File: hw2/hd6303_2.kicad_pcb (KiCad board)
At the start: 2 copper layers, 90.2 x 70.1 mm, 29 parts, among them J1 Conn_02x20_Odd_Even, J2 Conn_02x06_Odd_Even, J3 Screw_Terminal_01x02, SW1 SW_Push, U2 MAX708, U3 27C512, U4 HD6303RP, U5 HM62256BLP-7, U6 GAL16V8, Y1 4.9152M

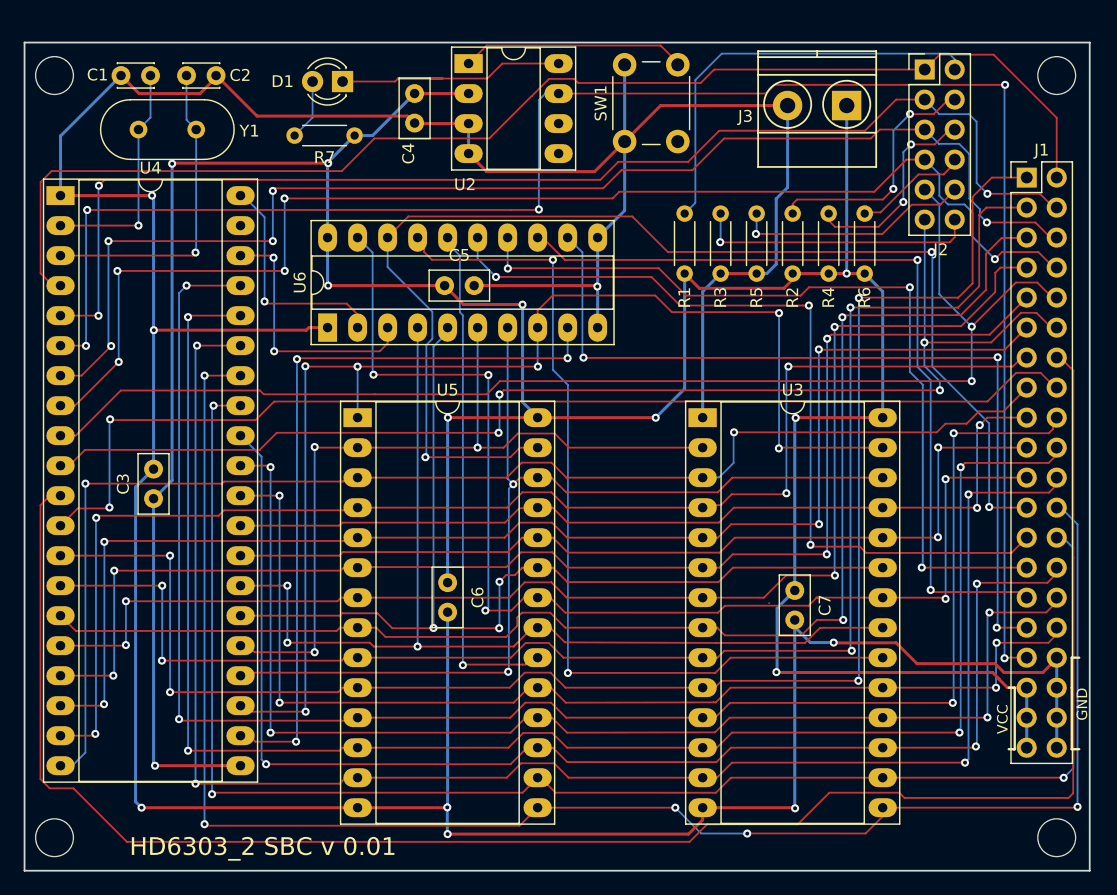
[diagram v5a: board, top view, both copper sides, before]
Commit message: reroute a couple of traces, silkscreen additions
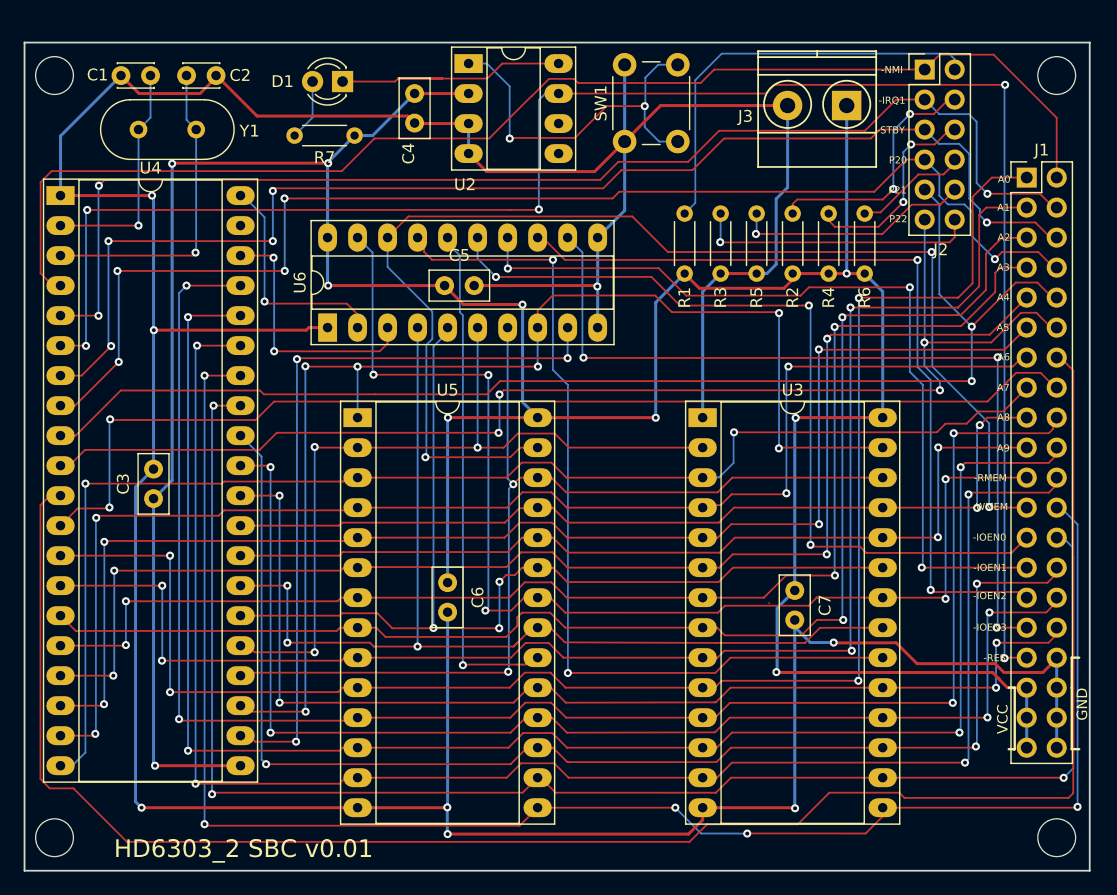
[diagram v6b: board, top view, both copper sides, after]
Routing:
- net Net-(SW1-Pad2): track 19.1 -> 32.3 mm, vias 0 -> 2
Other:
- board text added: "-IOEN0"
- board text added: "-IOEN1"
- board text added: "-IOEN2"
- board text added: "-IOEN3"
- board text added: "-IRQ1"
- board text added: "-NMI"
- board text added: "-RES"
- board text added: "-RMEM"
- board text added: "-STBY"
- board text added: "-WMEM"
- board text added: "A0"
- board text added: "A1"
- board text added: "A2"
- board text added: "A3"
- board text added: "A4"
- board text added: "A5"
- board text added: "A6"
- board text added: "A7"
- board text added: "A8"
- board text added: "A9"
- board text added: "HD6303_2 SBC v0.01"
- board text added: "P20"
- board text added: "P21"
- board text added: "P22"
- board text removed: "HD6303_2 SBC v 0.01"
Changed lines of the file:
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@@
-(kicad_pcb (version 4) (host pcbnew 4.0.7-e2-6376~58~ubuntu16.04.1)
+(kicad_pcb (version 4) (host pcbnew 4.0.2+dfsg1-stable)
   (general
     (links 155)
-    (no_connects 1)
-    (area 66.144857 85.645 178.203143 159.819)
+    (no_connects 0)
+    (area 66.069857 85.495 178.278143 159.719)
     (thickness 1.6)
-    (drawings 15)
-    (tracks 1157)
+    (drawings 38)
+    (tracks 1171)
     (zones 0)
     (modules 29)
@@
   )
   (setup
-    (last_trace_width 0.1524)
+    (last_trace_width 0.254)
     (user_trace_width 0.254)
     (trace_clearance 0.1524)
@@
     (pad 1 np_thru_hole circle (at 0 0) (size 3.2 3.2) (drill 3.2) (layers *.Cu *.Mask))
   )
+  (gr_text -RES (at 159.3342 139.7254) (layer F.SilkS)
+    (effects (font (size 0.6 0.6) (thickness 0.15)))
+  )
+  (gr_text -IOEN3 (at 158.9278 137.1346) (layer F.SilkS)
+    (effects (font (size 0.6 0.6) (thickness 0.15)))
+  )
+  (gr_text -IOEN2 (at 158.9278 134.4676) (layer F.SilkS)
+    (effects (font (size 0.6 0.6) (thickness 0.15)))
+  )
+  (gr_text -IOEN1 (at 158.9532 132.08) (layer F.SilkS)
+    (effects (font (size 0.6 0.6) (thickness 0.15)))
+  )
+  (gr_text -IOEN0 (at 158.9024 129.5146) (layer F.SilkS)
+    (effects (font (size 0.6 0.6) (thickness 0.15)))
+  )
+  (gr_text -WMEM (at 158.9532 126.9238) (layer F.SilkS)
+    (effects (font (size 0.6 0.6) (thickness 0.15)))
+  )
+  (gr_text -RMEM (at 158.9786 124.4854) (layer F.SilkS)
+    (effects (font (size 0.6 0.6) (thickness 0.15)))
+  )
+  (gr_text A8 (at 160.0962 119.3546) (layer F.SilkS)
+    (effects (font (size 0.6 0.6) (thickness 0.15)))
+  )
+  (gr_text A7 (at 160.0708 116.84) (layer F.SilkS)
+    (effects (font (size 0.6 0.6) (thickness 0.15)))
+  )
+  (gr_text A6 (at 160.0962 114.2492) (layer F.SilkS)
+    (effects (font (size 0.6 0.6) (thickness 0.15)))
+  )
+  (gr_text A5 (at 160.0454 111.76) (layer F.SilkS)
+    (effects (font (size 0.6 0.6) (thickness 0.15)))
+  )
+  (gr_text A4 (at 160.0708 109.1946) (layer F.SilkS)
+    (effects (font (size 0.6 0.6) (thickness 0.15)))
+  )
+  (gr_text A3 (at 160.0708 106.6546) (layer F.SilkS)
+    (effects (font (size 0.6 0.6) (thickness 0.15)))
+  )
+  (gr_text A2 (at 160.1216 104.1146) (layer F.SilkS)
+    (effects (font (size 0.6 0.6) (thickness 0.15)))
+  )
+  (gr_text A1 (at 160.0962 101.6) (layer F.SilkS)
+    (effects (font (size 0.6 0.6) (thickness 0.15)))
+  )
+  (gr_text A9 (at 160.0708 121.9708) (layer F.SilkS)
+    (effects (font (size 0.6 0.6) (thickness 0.15)))
+  )
+  (gr_text A0 (at 160.147 99.2124) (layer F.SilkS)
+    (effects (font (size 0.6 0.6) (thickness 0.15)))
+  )
+  (gr_text P22 (at 151.1808 102.5652) (layer F.SilkS)
+    (effects (font (size 0.6 0.6) (thickness 0.15)))
+  )
+  (gr_text P21 (at 151.13 100.1268) (layer F.SilkS)
+    (effects (font (size 0.6 0.6) (thickness 0.15)))
+  )
+  (gr_text P20 (at 151.1554 97.5868) (layer F.SilkS)
+    (effects (font (size 0.6 0.6) (thickness 0.15)))
+  )
+  (gr_text -STBY (at 150.5458 95.0468) (layer F.SilkS)
+    (effects (font (size 0.6 0.6) (thickness 0.15)))
+  )
+  (gr_text -IRQ1 (at 150.6474 92.5322) (layer F.SilkS)
+    (effects (font (size 0.6 0.6) (thickness 0.15)))
+  )
+  (gr_text -NMI (at 150.6474 89.9414) (layer F.SilkS)
+    (effects (font (size 0.6 0.6) (thickness 0.15)))
+  )
   (gr_line (start 161.036 147.447) (end 160.528 147.447) (angle 90) (layer F.SilkS) (width 0.2))
   (gr_line (start 161.036 147.447) (end 160.909 147.447) (angle 90) (layer F.SilkS) (width 0.2))
@@
     (effects (font (size 0.889 0.889) (thickness 0.22225)))
   )
-  (gr_text "HD6303_2 SBC v 0.01" (at 97.409 155.702) (layer F.SilkS)
+  (gr_text "HD6303_2 SBC v0.01" (at 95.758 155.8798) (layer F.SilkS)
     (effects (font (size 1.5 1.5) (thickness 0.3)))
   )
@@
   (segment (start 90.932 90.424) (end 90.932 94.18) (width 0.1524) (layer B.Cu) (net 3))
   (segment (start 90.932 94.18) (end 91.748 94.996) (width 0.1524) (layer B.Cu) (net 3))
-  (segment (start 133.096 107.188) (end 133.096 116.9416) (width 0.254) (layer B.Cu) (net 4))
-  (segment (start 130.63728 119.38) (end 120.65 119.38) (width 0.254) (layer F.Cu) (net 4))
+  (segment (start 130.64744 119.39016) (end 130.64744 109.63656) (width 0.254) (layer B.Cu) (net 4))
+  (via (at 130.64744 119.39016) (size 0.6858) (drill 0.3302) (layers F.Cu B.Cu) (net 4))
   (segment (start 130.64744 119.39016) (end 130.63728 119.38) (width 0.254) (layer F.Cu) (net 4))
-  (via (at 130.64744 119.39016) (size 0.6858) (drill 0.3302) (layers F.Cu B.Cu) (net 4))
-  (segment (start 133.096 116.9416) (end 130.64744 119.39016) (width 0.254) (layer B.Cu) (net 4))
+  (segment (start 120.65 119.38) (end 130.63728 119.38) (width 0.254) (layer F.Cu) (net 4))
+  (segment (start 130.64744 109.63656) (end 133.096 107.188) (width 0.254) (layer B.Cu) (net 4) (status 800000))
   (segment (start 120.65 119.38) (end 120.65 119.33936) (width 0.254) (layer B.Cu) (net 4))
   (segment (start 120.65 119.33936) (end 119.37492 118.06428) (width 0.254) (layer B.Cu) (net 4))
@@
   (segment (start 142.24 107.188) (end 142.24 107.696) (width 0.254) (layer F.Cu) (net 4))
   (segment (start 142.24 107.696) (end 141.5034 108.4326) (width 0.254) (layer F.Cu) (net 4))
+  (segment (start 141.5034 108.4326) (end 134.3406 108.4326) (width 0.254) (layer F.Cu) (net 4))
   (segment (start 134.3406 108.4326) (end 133.096 107.188) (width 0.254) (layer F.Cu) (net 4))
-  (segment (start 141.5034 108.4326) (end 134.3406 108.4326) (width 0.254) (layer F.Cu) (net 4))
   (segment (start 142.24 107.188) (end 145.288 107.188) (width 0.254) (layer F.Cu) (net 4))
   (segment (start 145.288 107.188) (end 146.812 107.188) (width 0.254) (layer F.Cu) (net 4))
@@
   (segment (start 155.5242 104.5464) (end 136.12368 104.5464) (width 0.1524) (layer F.Cu) (net 44))
   (segment (start 155.956 104.1146) (end 155.5242 104.5464) (width 0.1524) (layer F.Cu) (net 44))
+  (segment (start 129.7178 93.0148) (end 129.7178 94.7928) (width 0.1524) (layer B.Cu) (net 45))
+  (segment (start 130.937 96.012) (end 132.516 96.012) (width 0.1524) (layer B.Cu) (net 45) (status 800000))
+  (segment (start 129.7178 94.7928) (end 130.937 96.012) (width 0.1524) (layer B.Cu) (net 45))
+  (segment (start 114.808 89.408) (end 116.3574 89.408) (width 0.1524) (layer B.Cu) (net 45) (status 400000))
+  (segment (start 130.8584 89.512) (end 132.516 89.512) (width 0.1524) (layer B.Cu) (net 45) (status 800000))
+  (segment (start 129.7686 90.6018) (end 130.8584 89.512) (width 0.1524) (layer B.Cu) (net 45))
+  (segment (start 129.7686 92.964) (end 129.7686 90.6018) (width 0.1524) (layer B.Cu) (net 45))
+  (segment (start 129.7178 93.0148) (end 129.7686 92.964) (width 0.1524) (layer B.Cu) (net 45))
+  (via (at 129.7178 93.0148) (size 0.6858) (drill 0.3302) (layers F.Cu B.Cu) (net 45))
+  (segment (start 126.492 93.0148) (end 129.7178 93.0148) (width 0.1524) (layer F.Cu) (net 45))
+  (segment (start 123.7996 95.7072) (end 126.492 93.0148) (width 0.1524) (layer F.Cu) (net 45))
+  (segment (start 118.3386 95.7072) (end 123.7996 95.7072) (width 0.1524) (layer F.Cu) (net 45))
+  (segment (start 118.2878 95.758) (end 118.3386 95.7072) (width 0.1524) (layer F.Cu) (net 45))
+  (via (at 118.2878 95.758) (size 0.6858) (drill 0.3302) (layers F.Cu B.Cu) (net 45))
+  (segment (start 118.2878 91.3384) (end 118.2878 95.758) (width 0.1524) (layer B.Cu) (net 45))
+  (segment (start 116.3574 89.408) (end 118.2878 91.3384) (width 0.1524) (layer B.Cu) (net 45))
+  (segment (start 132.516 89.336) (end 132.516 89.512) (width 0.1524) (layer B.Cu) (net 45) (status C00000))
   (segment (start 132.516 89.512) (end 132.516 89.336) (width 0.1524) (layer F.Cu) (net 45))
-  (segment (start 132.516 89.336) (end 131.064 87.884) (width 0.1524) (layer F.Cu) (net 45))
-  (segment (start 131.064 87.884) (end 116.332 87.884) (width 0.1524) (layer F.Cu) (net 45))
-  (segment (start 116.332 87.884) (end 114.808 89.408) (width 0.1524) (layer F.Cu) (net 45))
   (segment (start 115.57 111.76) (end 115.57 121.92) (width 0.1524) (layer B.Cu) (net 48))
   (via (at 115.57 121.92) (size 0.6858) (drill 0.3302) (layers F.Cu B.Cu) (net 48))

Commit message: label expansion header pins
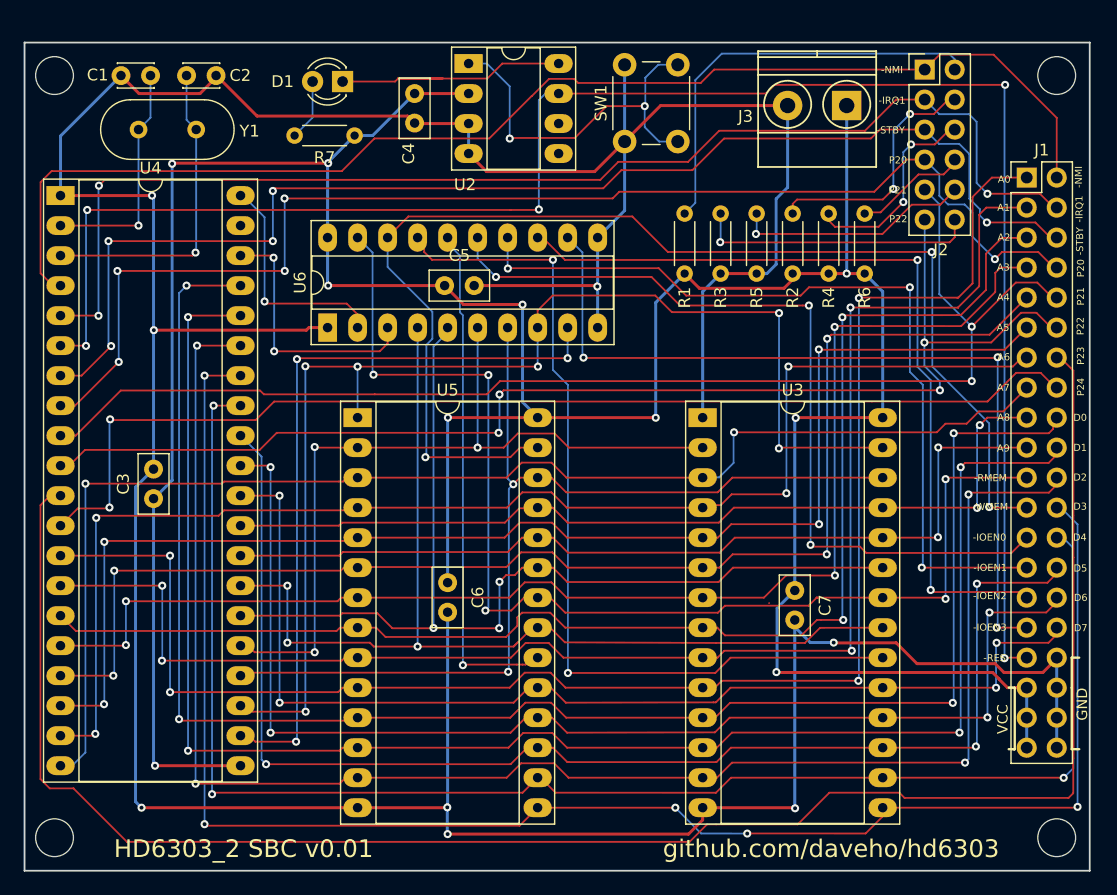
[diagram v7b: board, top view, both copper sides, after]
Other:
- board text added: "D0"
- board text added: "D1"
- board text added: "D2"
- board text added: "D3"
- board text added: "D4"
- board text added: "D5"
- board text added: "D6"
- board text added: "D7"
- board text added: "P23"
- board text added: "P24"
- board text added: "github.com/daveho/hd6303"
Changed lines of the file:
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@@
     (area 66.069857 85.495 178.278143 159.719)
     (thickness 1.6)
-    (drawings 38)
+    (drawings 55)
     (tracks 1171)
     (zones 0)
@@
     (pad 1 np_thru_hole circle (at 0 0) (size 3.2 3.2) (drill 3.2) (layers *.Cu *.Mask))
   )
+  (gr_text D7 (at 166.624 137.1854) (layer F.SilkS)
+    (effects (font (size 0.6 0.6) (thickness 0.15)))
+  )
+  (gr_text D6 (at 166.624 134.62) (layer F.SilkS)
+    (effects (font (size 0.6 0.6) (thickness 0.15)))
+  )
+  (gr_text D5 (at 166.5986 132.1308) (layer F.SilkS)
+    (effects (font (size 0.6 0.6) (thickness 0.15)))
+  )
+  (gr_text D4 (at 166.5478 129.5146) (layer F.SilkS)
+    (effects (font (size 0.6 0.6) (thickness 0.15)))
+  )
+  (gr_text D3 (at 166.5732 126.8984) (layer F.SilkS)
+    (effects (font (size 0.6 0.6) (thickness 0.15)))
+  )
+  (gr_text D2 (at 166.5732 124.4346) (layer F.SilkS)
+    (effects (font (size 0.6 0.6) (thickness 0.15)))
+  )
+  (gr_text D1 (at 166.5732 121.92) (layer F.SilkS)
+    (effects (font (size 0.6 0.6) (thickness 0.15)))
+  )
+  (gr_text D0 (at 166.5732 119.38) (layer F.SilkS)
+    (effects (font (size 0.6 0.6) (thickness 0.15)))
+  )
+  (gr_text P24 (at 166.624 116.7892 90) (layer F.SilkS)
+    (effects (font (size 0.6 0.6) (thickness 0.15)))
+  )
+  (gr_text P23 (at 166.624 114.1476 90) (layer F.SilkS)
+    (effects (font (size 0.6 0.6) (thickness 0.15)))
+  )
+  (gr_text P22 (at 166.5986 111.633 90) (layer F.SilkS)
+    (effects (font (size 0.6 0.6) (thickness 0.15)))
+  )
+  (gr_text P21 (at 166.624 109.1184 90) (layer F.SilkS)
+    (effects (font (size 0.6 0.6) (thickness 0.15)))
+  )
+  (gr_text P20 (at 166.624 106.7308 90) (layer F.SilkS)
+    (effects (font (size 0.6 0.6) (thickness 0.15)))
+  )
+  (gr_text -STBY (at 166.5478 104.4448 90) (layer F.SilkS)
+    (effects (font (size 0.6 0.6) (thickness 0.15)))
+  )
+  (gr_text -IRQ1 (at 166.497 101.727 90) (layer F.SilkS)
+    (effects (font (size 0.6 0.6) (thickness 0.15)))
+  )
+  (gr_text -NMI (at 166.4462 99.0092 90) (layer F.SilkS)
+    (effects (font (size 0.6 0.6) (thickness 0.15)))
+  )
+  (gr_text github.com/daveho/hd6303 (at 145.4912 155.8798) (layer F.SilkS)
+    (effects (font (size 1.5 1.5) (thickness 0.3)))
+  )
   (gr_text -RES (at 159.3342 139.7254) (layer F.SilkS)
